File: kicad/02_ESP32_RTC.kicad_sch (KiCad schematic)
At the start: 32 parts, among them SW1 RESET, SW2 BOOT, U4 ESP32-S3-WROOM-1U-N16R8, U5 TPS3808G33DBVR, U6 RV-8263-C8

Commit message: Phase 2: complete schematic with review and netlist check
Draw the 5-sheet hierarchical schematic (power, ESP32/RTC,
AUTOTERM/1-Wire, button/indicators). ERC clean except one justified
footprint-filter warning, exported netlist matches all expected nodes,
SPICE values are numeric and non-simulated parts carry a reason. Add
BOM fields, final design document and phase 2 review.

Co-Authored-By: Claude Opus 5.5 <noreply@anthropic.com>
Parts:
- BT1: LCSC (none) -> C20606803; MPN (none) -> MY-1225-01-J; Manufacturer (none) -> MYOUNG; Spez (none) -> Zelle Panasonic BR1225 wird nicht bestueckt
- C12, C13: Spez (none) -> X7R 10 V 1206
- C14, C15, C16, C19: Spez (none) -> X7R 16 V 0603
- C17, C18: value DNP -> 10pF; Spez (none) -> DNP, C0G 50 V 0603; now not fitted
- D5, D6: LCSC (none) -> C48502; MPN (none) -> BAS116,215; Manufacturer (none) -> Nexperia
- R10: renamed from R11; Spez (none) -> 0603, 1 %, 0,1 W
- R11: renamed from R12; Spez (none) -> 0603, 1 %, 0,1 W
- R12: renamed from R13; Spez (none) -> 0603, 1 %, 0,1 W
- R13: renamed from R14; Spez (none) -> 0603, 1 %, 0,1 W
- R14: renamed from R15; Spez (none) -> 0603, 1 %, 0,1 W
- R7: renamed from R8; Spez (none) -> 0603, 1 %, 0,1 W
- R8: renamed from R9; Spez (none) -> 0603, 1 %, 0,1 W
- R9: renamed from R10; Spez (none) -> 0603, 1 %, 0,1 W
- SW1, SW2: LCSC (none) -> C72443; MPN (none) -> KMR221GLFS; Manufacturer (none) -> C&K
- TP10, TP11, TP12, TP13, TP14, TP15, TP8, TP9: now left out of the parts list
- U4: LCSC (none) -> C3013946; MPN (none) -> ESP32-S3-WROOM-1U-N16R8; Manufacturer (none) -> Espressif
- U5: LCSC (none) -> C51886189; MPN (none) -> TPS3808G33DBVR; Manufacturer (none) -> Texas Instruments
- U6: LCSC (none) -> C24955831; MPN (none) -> RV-8263-C8-32.768KHZ-20PPM-TA-QC; Manufacturer (none) -> Micro Crystal
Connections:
- net RTC_VDD: now reaches C19.1, D5.3 (K), D6.3 (K), U6.5 (VDD)
- net BOOT_N: now reaches R8.2, SW2.2, TP9.1, U4.27 (IO0)
- net EN: now reaches C15.1, R7.2, SW1.2, TP8.1, U4.3 (EN), U5.1 (~{RESET})
- net VBAT: now reaches BT1.1 (+), D6.1 (A)

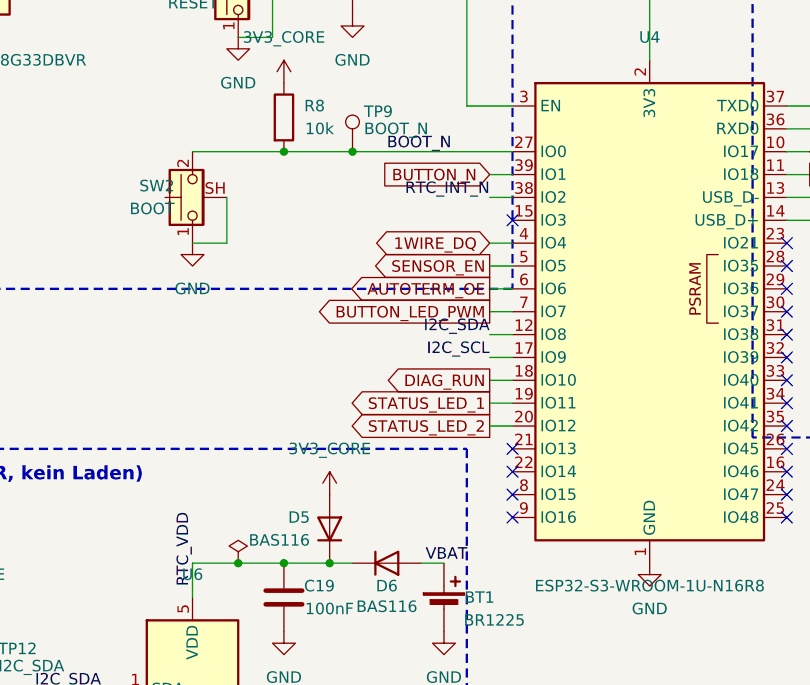
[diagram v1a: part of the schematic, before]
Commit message: Rework Rev B placement for short connections and layout checklist
- Reassign ESP32 GPIOs so each block sits at the module edge facing it
  (schematic, requirements A12 v2.1, firmware note P2-04)
- Connectivity-driven placement: decoupling within 2 mm of its pin, USB
  series resistors at the module, ESD parts at their connectors, diagnostic
  LEDs in one row; total connection length 1377 -> 729 mm
- Connector order J1, J2, J4, J3; three fiducials; Power net class 0.65 mm
- Layout checklist B7 from Espressif, TI, JLCPCB and EMC guidance

Co-Authored-By: Claude Opus 5.5 <noreply@anthropic.com>
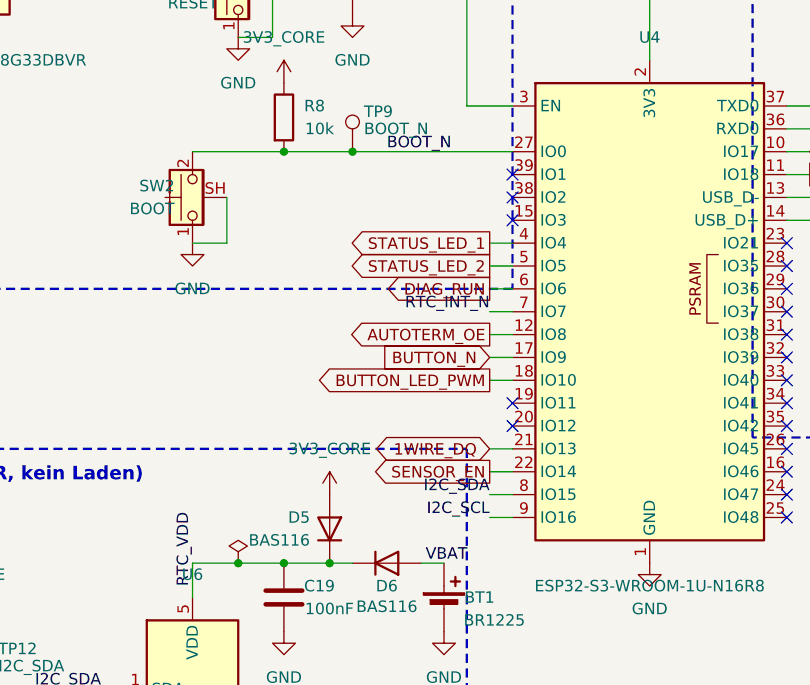
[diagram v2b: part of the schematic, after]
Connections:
- net 1WIRE_DQ: now also U4.21 (IO13); no longer U4.4 (IO4)
- net AUTOTERM_OE: now also U4.12 (IO8); no longer U4.6 (IO6)
- net BUTTON_LED_PWM: now also U4.18 (IO10); no longer U4.7 (IO7)
- net BUTTON_N: now also U4.17 (IO9); no longer U4.39 (IO1)
- net DIAG_RUN: now also U4.6 (IO6); no longer U4.18 (IO10)
- net I2C_SCL: now also U4.9 (IO16); no longer U4.17 (IO9)
- net I2C_SDA: now also U4.8 (IO15); no longer U4.12 (IO8)
- net RTC_INT_N: now also U4.7 (IO7); no longer U4.38 (IO2)
- net SENSOR_EN: now also U4.22 (IO14); no longer U4.5 (IO5)
- net STATUS_LED_1: now also U4.4 (IO4); no longer U4.19 (IO11)
- net STATUS_LED_2: now also U4.5 (IO5); no longer U4.20 (IO12)
